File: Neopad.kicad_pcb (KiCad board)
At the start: 2 copper layers, 99.2 x 87.3 mm, 34 parts, among them SW1 Rotary_Encoder_Switch, SW2 SW_MEC_5E, SW3 Rotary_Encoder_Switch, U1 ProMicro

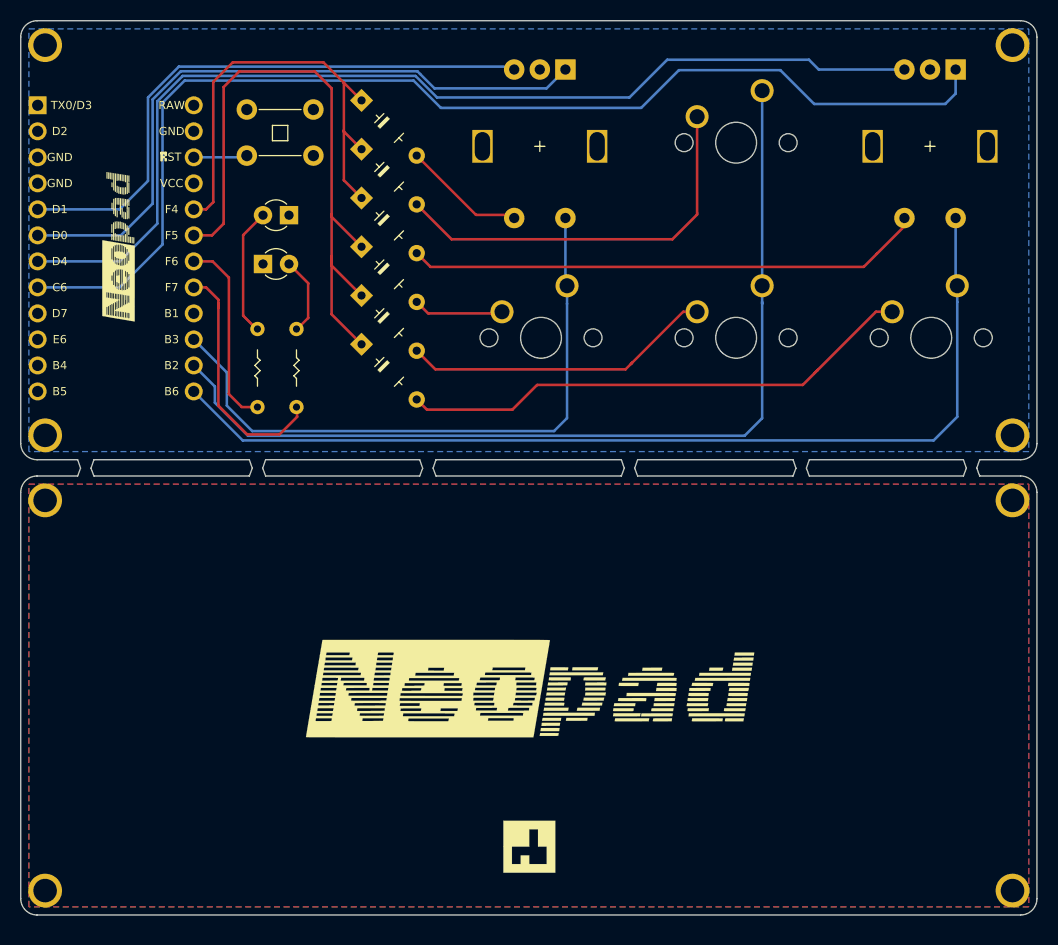
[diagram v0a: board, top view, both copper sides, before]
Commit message: PCB revision for manufacturing improvement
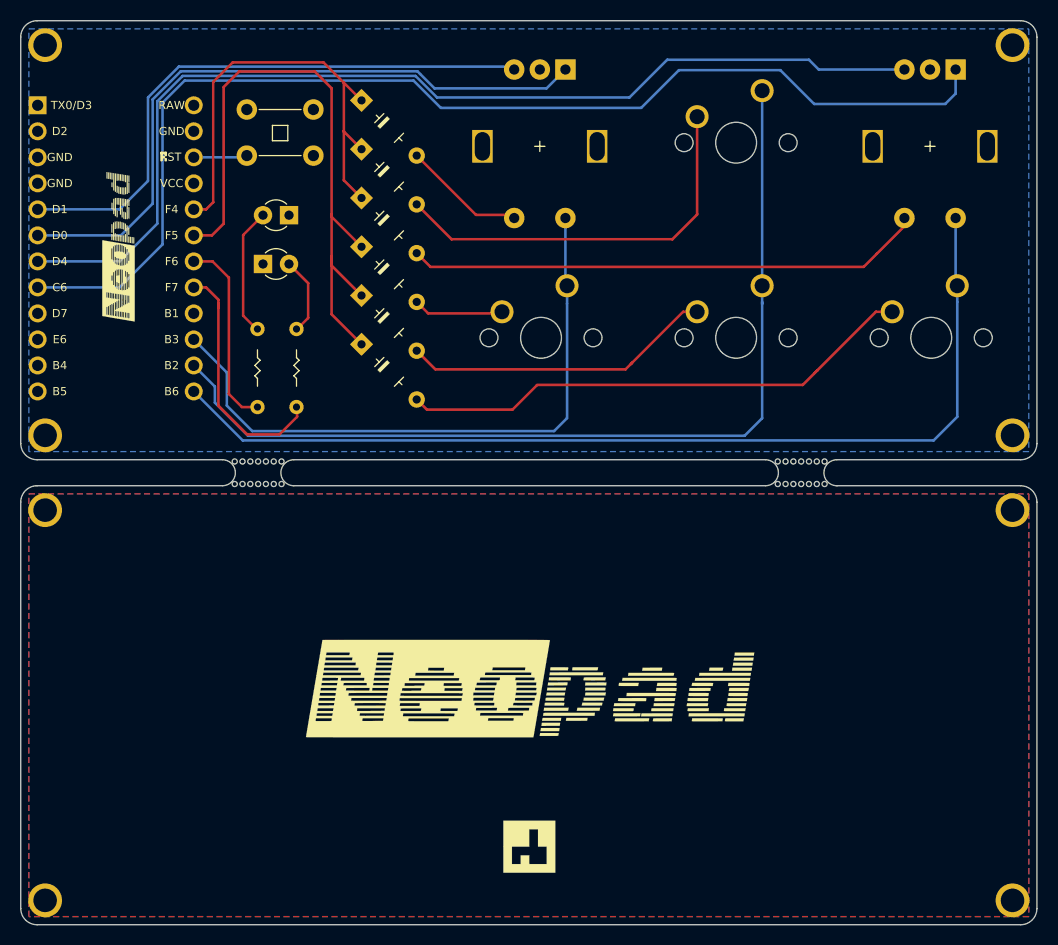
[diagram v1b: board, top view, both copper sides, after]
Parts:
- added G***: LOGO, Logocustom:rookiebwoy-web, B.Cu at (111.1, 69.8)
- added mouse-bite-2.54mm-slot: VAL**, rookiebwoy:MouseBite-H2.54mm-W4.57mm, F.Cu at (117.5, 94.9)
- added mouse-bite-2.54mm-slot: VAL**, rookiebwoy:MouseBite-H2.54mm-W4.57mm, F.Cu at (64.5, 94.9)
- moved H6 0.95 mm to (43.7, 136.7)
- moved H8 0.95 mm to (138.1, 136.7)
- moved H5 0.95 mm to (43.7, 98.6)
- moved H7 0.95 mm to (138.1, 98.6)
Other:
- board size 99.2 x 87.3 mm -> 99.2 x 88.3 mm
